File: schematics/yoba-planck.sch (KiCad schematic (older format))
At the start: 54 parts, among them M1 AUDIO-JACK3, M2 AUDIO-JACK3, M3 ARDUINO_PRO_MICRO, SW1 SW_PUSH, SW10 SW_PUSH, SW11 SW_PUSH, SW12 SW_PUSH, SW13 SW_PUSH, SW14 SW_PUSH, SW15 SW_PUSH, SW16 SW_PUSH, SW17 SW_PUSH, SW18 SW_PUSH, SW19 SW_PUSH, SW2 SW_PUSH, SW20 SW_PUSH, SW21 SW_PUSH, SW22 SW_PUSH, SW23 SW_PUSH, SW24 SW_PUSH, SW3 SW_PUSH, SW4 SW_PUSH, SW5 SW_PUSH, SW6 SW_PUSH, SW7 SW_PUSH, SW8 SW_PUSH, SW9 SW_PUSH

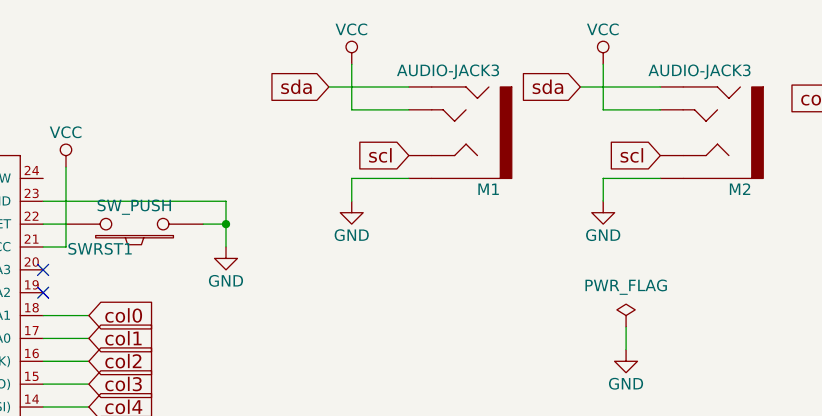
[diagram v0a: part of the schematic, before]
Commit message: series resistance added to i2c bus
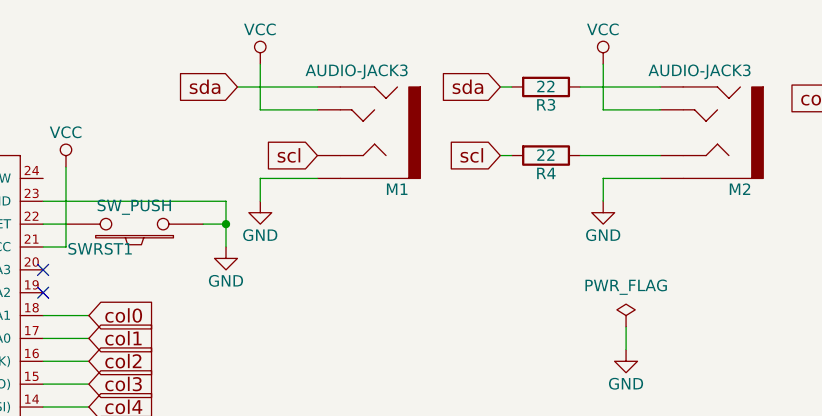
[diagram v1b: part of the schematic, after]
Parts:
- added R3, R4: 22, symbol R
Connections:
- net scl: now also R4.2; no longer M2.3 (RNG1)
- net sda: now also R3.2; no longer M2.2 (RNG2)
- new net: M2.2 (RNG2), R3.1
- new net: M2.3 (RNG1), R4.1
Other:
- moved on the sheet: M1
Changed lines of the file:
@@
 $EndComp
 $Comp
-L GND #PWR01
+L GND #PWR3
 U 1 1 58C7AB40
 P 4100 1500
-F 0 "#PWR01" H 4100 1250 50  0001 C CNN
+F 0 "#PWR3" H 4100 1250 50  0001 C CNN
 F 1 "GND" H 4100 1350 50  0000 C CNN
 F 2 "" H 4100 1500 50  0000 C CNN
@@
 $EndComp
 $Comp
-L VCC #PWR02
+L VCC #PWR4
 U 1 1 58C80AC6
-P 4650 700
-F 0 "#PWR02" H 4650 550 50  0001 C CNN
-F 1 "VCC" H 4650 850 50  0000 C CNN
-F 2 "" H 4650 700 50  0000 C CNN
-F 3 "" H 4650 700 50  0000 C CNN
-	1    4650 700
-	1    0    0    -1
-$EndComp
-Wire Wire Line
-	4650 700  4650 900
-$Comp
-L GND #PWR03
+P 4250 700
+F 0 "#PWR4" H 4250 550 50  0001 C CNN
+F 1 "VCC" H 4250 850 50  0000 C CNN
+F 2 "" H 4250 700 50  0000 C CNN
+F 3 "" H 4250 700 50  0000 C CNN
+	1    4250 700
+	1    0    0    -1
+$EndComp
+Wire Wire Line
+	4250 700  4250 900
+$Comp
+L GND #PWR5
 U 1 1 58C80C56
-P 4650 1300
-F 0 "#PWR03" H 4650 1050 50  0001 C CNN
-F 1 "GND" H 4650 1150 50  0000 C CNN
-F 2 "" H 4650 1300 50  0000 C CNN
-F 3 "" H 4650 1300 50  0000 C CNN
-	1    4650 1300
-	1    0    0    -1
-$EndComp
-Wire Wire Line
-	4900 1200 4650 1200
-Wire Wire Line
-	4650 1200 4650 1300
+P 4250 1300
+F 0 "#PWR5" H 4250 1050 50  0001 C CNN
+F 1 "GND" H 4250 1150 50  0000 C CNN
+F 2 "" H 4250 1300 50  0000 C CNN
+F 3 "" H 4250 1300 50  0000 C CNN
+	1    4250 1300
+	1    0    0    -1
+$EndComp
+Wire Wire Line
+	4500 1200 4250 1200
+Wire Wire Line
+	4250 1200 4250 1300
 Text GLabel 1950 1600 0    60   Input ~ 0
 sda
-Text GLabel 4900 1100 0    60   Input ~ 0
+Text GLabel 4500 1100 0    60   Input ~ 0
 scl
-Text GLabel 4550 800  0    60   Input ~ 0
+Text GLabel 4150 800  0    60   Input ~ 0
 sda
 $Comp
-L GND #PWR04
+L GND #PWR8
 U 1 1 58C8646C
 P 5850 1950
-F 0 "#PWR04" H 5850 1700 50  0001 C CNN
+F 0 "#PWR8" H 5850 1700 50  0001 C CNN
 F 1 "GND" H 5850 1800 50  0000 C CNN
 F 2 "" H 5850 1950 50  0000 C CNN
@@
 $EndComp
 $Comp
-L PWR_FLAG #FLG05
+L PWR_FLAG #FLG1
 U 1 1 58C86543
 P 5850 1850
-F 0 "#FLG05" H 5850 1945 50  0001 C CNN
+F 0 "#FLG1" H 5850 1945 50  0001 C CNN
 F 1 "PWR_FLAG" H 5850 2030 50  0000 C CNN
 F 2 "" H 5850 1850 50  0000 C CNN
@@
 	5850 1850 5850 1950
 Wire Wire Line
-	4650 900  4900 900
-Wire Wire Line
-	4550 800  4900 800
+	4250 900  4500 900
+Wire Wire Line
+	4150 800  4500 800
 $Comp
 L AUDIO-JACK3 M1
 U 1 1 58C9EB5E
-P 5100 1000
-F 0 "M1" H 4900 1220 50  0000 L BNN
-F 1 "AUDIO-JACK3" H 4900 700 50  0000 L BNN
-F 2 "yoba:TRRS-ebay" H 5130 1150 20  0001 C CNN
-F 3 "" H 5100 1000 60  0001 C CNN
-	1    5100 1000
+P 4700 1000
+F 0 "M1" H 4500 1220 50  0000 L BNN
+F 1 "AUDIO-JACK3" H 4500 700 50  0000 L BNN
+F 2 "yoba:TRRS-ebay" H 4730 1150 20  0001 C CNN
+F 3 "" H 4700 1000 60  0001 C CNN
+	1    4700 1000
 	-1   0    0    1
 $EndComp
@@
 	1950 1700 2400 1700
 $Comp
-L VCC #PWR06
+L VCC #PWR1
 U 1 1 58CA693D
 P 2100 1050
-F 0 "#PWR06" H 2100 900 50  0001 C CNN
+F 0 "#PWR1" H 2100 900 50  0001 C CNN
 F 1 "VCC" H 2100 1200 50  0000 C CNN
 F 2 "" H 2100 1050 50  0000 C CNN
@@
 Connection ~ 2100 1150
 $Comp
-L VCC #PWR07
+L VCC #PWR2
 U 1 1 58CA85FA
 P 3400 1150
-F 0 "#PWR07" H 3400 1000 50  0001 C CNN
+F 0 "#PWR2" H 3400 1000 50  0001 C CNN
 F 1 "VCC" H 3400 1300 50  0000 C CNN
 F 2 "" H 3400 1150 50  0000 C CNN
@@
 NoConn ~ 2400 1800
 $Comp
-L VCC #PWR08
+L VCC #PWR6
 U 1 1 58D178D3
 P 5750 700
-F 0 "#PWR08" H 5750 550 50  0001 C CNN
+F 0 "#PWR6" H 5750 550 50  0001 C CNN
 F 1 "VCC" H 5750 850 50  0000 C CNN
 F 2 "" H 5750 700 50  0000 C CNN
@@
 	5750 700  5750 900
 $Comp
-L GND #PWR09
+L GND #PWR7
 U 1 1 58D178DA
 P 5750 1300
-F 0 "#PWR09" H 5750 1050 50  0001 C CNN
+F 0 "#PWR7" H 5750 1050 50  0001 C CNN
 F 1 "GND" H 5750 1150 50  0000 C CNN
 F 2 "" H 5750 1300 50  0000 C CNN
@@
 Wire Wire Line
 	5750 1200 5750 1300
-Text GLabel 6000 1100 0    60   Input ~ 0
+Text GLabel 5300 1100 0    60   Input ~ 0
 scl
-Text GLabel 5650 800  0    60   Input ~ 0
+Text GLabel 5300 800  0    60   Input ~ 0
 sda
 Wire Wire Line
@@
 $EndComp
 NoConn ~ 2400 1900
+$Comp
+L R R3
+U 1 1 58DBF535
+P 5500 800
+F 0 "R3" V 5580 800 50  0000 C CNN
+F 1 "22" V 5500 800 50  0000 C CNN
+F 2 "" V 5430 800 50  0000 C CNN
+F 3 "" H 5500 800 50  0000 C CNN
+	1    5500 800
+	0    1    1    0
+$EndComp
+Wire Wire Line
+	5350 800  5300 800
+$Comp
+L R R4
+U 1 1 58DBFD81
+P 5500 1100
+F 0 "R4" V 5580 1100 50  0000 C CNN
+F 1 "22" V 5500 1100 50  0000 C CNN
+F 2 "" V 5430 1100 50  0000 C CNN
+F 3 "" H 5500 1100 50  0000 C CNN
+	1    5500 1100
+	0    1    1    0
+$EndComp
+Wire Wire Line
+	5300 1100 5350 1100
+Wire Wire Line
+	5650 1100 6000 1100
 $EndSCHEMATC

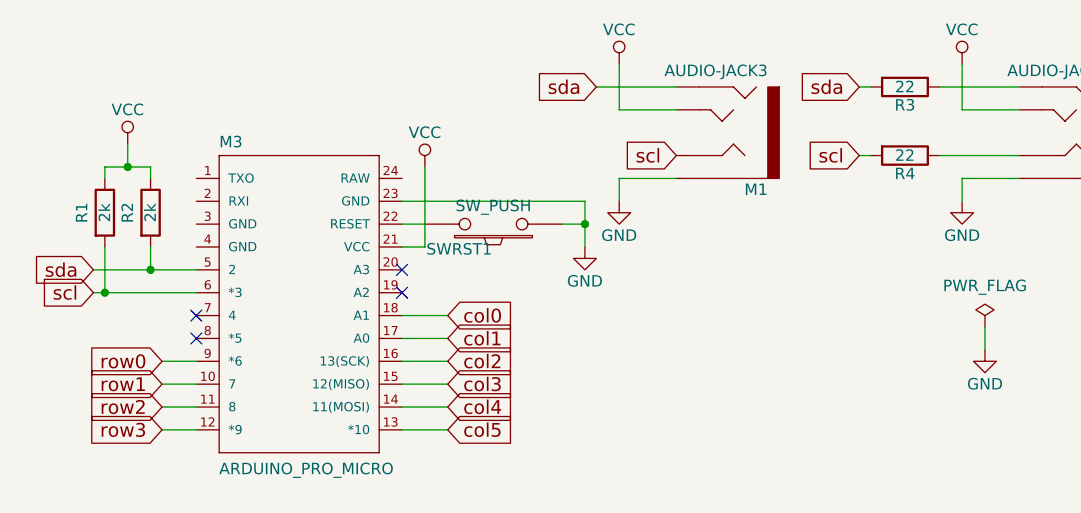
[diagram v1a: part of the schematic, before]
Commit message: Logo updated, layout improoved, mouting holes enlarged
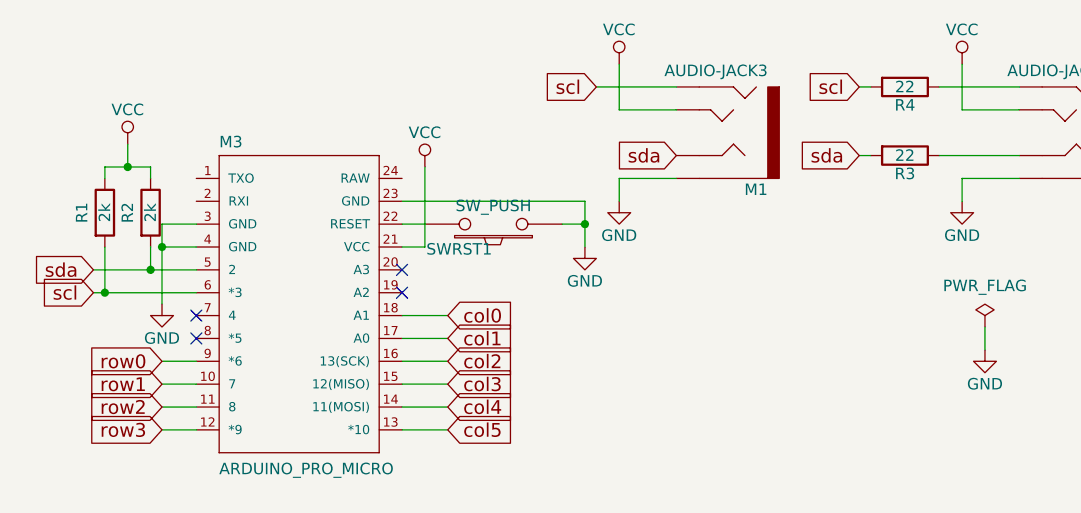
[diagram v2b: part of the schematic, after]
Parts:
- M3: footprint SparkFun-Boards:ARDUINO_PRO_MICRO -> yoba:ARDUINO_PRO_MICRO
- R3, R4: footprint (none) -> Resistors_SMD:R_0805_HandSoldering
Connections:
- net GND: now also M3.3 (GND), M3.4 (GND)
- net scl: now also M1.2 (RNG2); no longer M1.3 (RNG1)
- net sda: now also M1.3 (RNG1); no longer M1.2 (RNG2)
- net at M2.2 (RNG2): now also R4.1; no longer R3.1
- net at M2.3 (RNG1): now also R3.1; no longer R4.1
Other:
- moved on the sheet: R3, R4
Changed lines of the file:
@@
 $EndComp
 $Comp
-L GND #PWR3
+L GND #PWR01
 U 1 1 58C7AB40
 P 4100 1500
-F 0 "#PWR3" H 4100 1250 50  0001 C CNN
+F 0 "#PWR01" H 4100 1250 50  0001 C CNN
 F 1 "GND" H 4100 1350 50  0000 C CNN
 F 2 "" H 4100 1500 50  0000 C CNN
@@
 $EndComp
 $Comp
-L VCC #PWR4
+L VCC #PWR02
 U 1 1 58C80AC6
 P 4250 700
-F 0 "#PWR4" H 4250 550 50  0001 C CNN
+F 0 "#PWR02" H 4250 550 50  0001 C CNN
 F 1 "VCC" H 4250 850 50  0000 C CNN
 F 2 "" H 4250 700 50  0000 C CNN
@@
 	4250 700  4250 900
 $Comp
-L GND #PWR5
+L GND #PWR03
 U 1 1 58C80C56
 P 4250 1300
-F 0 "#PWR5" H 4250 1050 50  0001 C CNN
+F 0 "#PWR03" H 4250 1050 50  0001 C CNN
 F 1 "GND" H 4250 1150 50  0000 C CNN
 F 2 "" H 4250 1300 50  0000 C CNN
@@
 Text GLabel 1950 1600 0    60   Input ~ 0
 sda
+Text GLabel 4150 800  0    60   Input ~ 0
+scl
 Text GLabel 4500 1100 0    60   Input ~ 0
-scl
-Text GLabel 4150 800  0    60   Input ~ 0
 sda
 $Comp
-L GND #PWR8
+L GND #PWR04
 U 1 1 58C8646C
 P 5850 1950
-F 0 "#PWR8" H 5850 1700 50  0001 C CNN
+F 0 "#PWR04" H 5850 1700 50  0001 C CNN
 F 1 "GND" H 5850 1800 50  0000 C CNN
 F 2 "" H 5850 1950 50  0000 C CNN
@@
 $EndComp
 $Comp
-L PWR_FLAG #FLG1
+L PWR_FLAG #FLG05
 U 1 1 58C86543
 P 5850 1850
-F 0 "#FLG1" H 5850 1945 50  0001 C CNN
+F 0 "#FLG05" H 5850 1945 50  0001 C CNN
 F 1 "PWR_FLAG" H 5850 2030 50  0000 C CNN
 F 2 "" H 5850 1850 50  0000 C CNN
@@
 	1950 1700 2400 1700
 $Comp
-L VCC #PWR1
+L VCC #PWR06
 U 1 1 58CA693D
 P 2100 1050
-F 0 "#PWR1" H 2100 900 50  0001 C CNN
+F 0 "#PWR06" H 2100 900 50  0001 C CNN
 F 1 "VCC" H 2100 1200 50  0000 C CNN
 F 2 "" H 2100 1050 50  0000 C CNN
@@
 Connection ~ 2100 1150
 $Comp
-L VCC #PWR2
+L VCC #PWR07
 U 1 1 58CA85FA
 P 3400 1150
-F 0 "#PWR2" H 3400 1000 50  0001 C CNN
+F 0 "#PWR07" H 3400 1000 50  0001 C CNN
 F 1 "VCC" H 3400 1300 50  0000 C CNN
 F 2 "" H 3400 1150 50  0000 C CNN
@@
 NoConn ~ 2400 1800
 $Comp
-L VCC #PWR6
+L VCC #PWR08
 U 1 1 58D178D3
 P 5750 700
-F 0 "#PWR6" H 5750 550 50  0001 C CNN
+F 0 "#PWR08" H 5750 550 50  0001 C CNN
 F 1 "VCC" H 5750 850 50  0000 C CNN
 F 2 "" H 5750 700 50  0000 C CNN
@@
 	5750 700  5750 900
 $Comp
-L GND #PWR7
+L GND #PWR09
 U 1 1 58D178DA
 P 5750 1300
-F 0 "#PWR7" H 5750 1050 50  0001 C CNN
+F 0 "#PWR09" H 5750 1050 50  0001 C CNN
 F 1 "GND" H 5750 1150 50  0000 C CNN
 F 2 "" H 5750 1300 50  0000 C CNN
@@
 Wire Wire Line
 	5750 1200 5750 1300
+Text GLabel 5300 800  0    60   Input ~ 0
+scl
 Text GLabel 5300 1100 0    60   Input ~ 0
-scl
-Text GLabel 5300 800  0    60   Input ~ 0
 sda
 Wire Wire Line
@@
 F 0 "M3" H 2500 2530 50  0000 L BNN
 F 1 "ARDUINO_PRO_MICRO" H 2500 1100 50  0000 L BNN
-F 2 "SparkFun-Boards:ARDUINO_PRO_MICRO" H 2830 1950 20  0001 C CNN
+F 2 "yoba:ARDUINO_PRO_MICRO" H 2830 1950 20  0001 C CNN
 F 3 "" H 2800 1800 60  0001 C CNN
 	1    2800 1800
@@
 L R R3
 U 1 1 58DBF535
+P 5500 1100
+F 0 "R3" V 5580 1100 50  0000 C CNN
+F 1 "22" V 5500 1100 50  0000 C CNN
+F 2 "Resistors_SMD:R_0805_HandSoldering" V 5430 1100 50  0001 C CNN
+F 3 "" H 5500 1100 50  0000 C CNN
+	1    5500 1100
+	0    1    1    0
+$EndComp
+Wire Wire Line
+	5350 800  5300 800
+$Comp
+L R R4
+U 1 1 58DBFD81
 P 5500 800
-F 0 "R3" V 5580 800 50  0000 C CNN
+F 0 "R4" V 5580 800 50  0000 C CNN
 F 1 "22" V 5500 800 50  0000 C CNN
-F 2 "" V 5430 800 50  0000 C CNN
+F 2 "Resistors_SMD:R_0805_HandSoldering" V 5430 800 50  0001 C CNN
 F 3 "" H 5500 800 50  0000 C CNN
 	1    5500 800
@@
 $EndComp
 Wire Wire Line
-	5350 800  5300 800
-$Comp
-L R R4
-U 1 1 58DBFD81
-P 5500 1100
-F 0 "R4" V 5580 1100 50  0000 C CNN
-F 1 "22" V 5500 1100 50  0000 C CNN
-F 2 "" V 5430 1100 50  0000 C CNN
-F 3 "" H 5500 1100 50  0000 C CNN
-	1    5500 1100
-	0    1    1    0
-$EndComp
-Wire Wire Line
 	5300 1100 5350 1100
 Wire Wire Line
 	5650 1100 6000 1100
+$Comp
+L GND #PWR010
+U 1 1 58DC02E5
+P 2250 1750
+F 0 "#PWR010" H 2250 1500 50  0001 C CNN
+F 1 "GND" H 2250 1600 50  0000 C CNN
+F 2 "" H 2250 1750 50  0000 C CNN
+F 3 "" H 2250 1750 50  0000 C CNN
+	1    2250 1750
+	1    0    0    -1
+$EndComp
+Wire Wire Line
+	2400 1400 2250 1400
+Wire Wire Line
+	2250 1400 2250 1750
+Wire Wire Line
+	2400 1500 2250 1500
+Connection ~ 2250 1500
 $EndSCHEMATC

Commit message: rev2
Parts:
- added C1: C, Capacitors_SMD:C_0805_HandSoldering, symbol C
- added D25, D26, D27, D28, D29, D30, D31, D32, D33, D34, D35, D36, D37, D38, D39, D40, D41, D42, D43, D44, D45, D46, D47, D48: LED, mx1a:MX1A-led, symbol LED
- added Q1: BS170, TO_SOT_Packages_SMD:SOT-23_Handsoldering, symbol BS170
- added R10, R11, R12, R13, R14, R15, R16, R17, R18, R19, R20, R21, R22, R23, R24, R25, R26, R27, R28, R5, R6, R7, R8, R9: 1k, Resistors_SMD:R_0805_HandSoldering, symbol R
- renumbered SWRST1 to RST1
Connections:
- net GND: now also C1.1, Q1.3 (S)
- net VCC: now also D25.2 (A), D26.2 (A), D27.2 (A), D28.2 (A), D29.2 (A), D30.2 (A), D31.2 (A), D32.2 (A), D33.2 (A), D34.2 (A), D35.2 (A), D36.2 (A), D37.2 (A), D38.2 (A), D39.2 (A), D40.2 (A), D41.2 (A), D42.2 (A), D43.2 (A), D44.2 (A), D45.2 (A), D46.2 (A), D47.2 (A), D48.2 (A)
- net row0: now also D1.1 (K), D13.1 (K), D17.1 (K), D21.1 (K), D5.1 (K), D9.1 (K); no longer D1.2 (A), D13.2 (A), D17.2 (A), D21.2 (A), D5.2 (A), D9.2 (A)
- net row1: now also D10.1 (K), D14.1 (K), D18.1 (K), D2.1 (K), D22.1 (K), D6.1 (K); no longer D10.2 (A), D14.2 (A), D18.2 (A), D2.2 (A), D22.2 (A), D6.2 (A)
- net row2: now also D11.1 (K), D15.1 (K), D19.1 (K), D23.1 (K), D3.1 (K), D7.1 (K); no longer D11.2 (A), D15.2 (A), D19.2 (A), D23.2 (A), D3.2 (A), D7.2 (A)
- net row3: now also D12.1 (K), D16.1 (K), D20.1 (K), D24.1 (K), D4.1 (K), D8.1 (K); no longer D12.2 (A), D16.2 (A), D20.2 (A), D24.2 (A), D4.2 (A), D8.2 (A)
- net scl: no longer M1.2 (RNG2), R1.2
- net sda: no longer M1.3 (RNG1), R2.2
- net at SW1.2: now also D1.2 (A); no longer D1.1 (K)
- net at SW5.2: now also D5.2 (A); no longer D5.1 (K)
- net at SW9.2: now also D9.2 (A); no longer D9.1 (K)
- net at SW13.2: now also D13.2 (A); no longer D13.1 (K)
- net at SW17.2: now also D17.2 (A); no longer D17.1 (K)
- net at SW21.2: now also D21.2 (A); no longer D21.1 (K)
- net at SW2.2: now also D2.2 (A); no longer D2.1 (K)
- net at SW6.2: now also D6.2 (A); no longer D6.1 (K)
- net at SW10.2: now also D10.2 (A); no longer D10.1 (K)
- net at SW14.2: now also D14.2 (A); no longer D14.1 (K)
- net at SW18.2: now also D18.2 (A); no longer D18.1 (K)
- net at SW22.2: now also D22.2 (A); no longer D22.1 (K)
- net at SW3.2: now also D3.2 (A); no longer D3.1 (K)
- net at SW7.2: now also D7.2 (A); no longer D7.1 (K)
- net at SW11.2: now also D11.2 (A); no longer D11.1 (K)
- net at SW15.2: now also D15.2 (A); no longer D15.1 (K)
- net at SW19.2: now also D19.2 (A); no longer D19.1 (K)
- net at SW23.2: now also D23.2 (A); no longer D23.1 (K)
- net at SW4.2: now also D4.2 (A); no longer D4.1 (K)
- net at SW8.2: now also D8.2 (A); no longer D8.1 (K)
- net at SW12.2: now also D12.2 (A); no longer D12.1 (K)
- net at SW16.2: now also D16.2 (A); no longer D16.1 (K)
- net at SW20.2: now also D20.2 (A); no longer D20.1 (K)
- net at SW24.2: now also D24.2 (A); no longer D24.1 (K)
- net at M3.22 (RESET), RST1.2: now also C1.2
- net backlight: now reaches M3.8 (*5)
- net backlight: now also Q1.2 (G)
- net at M2.2 (RNG2), R4.1: now also M1.2 (RNG2), R1.2
- net at M2.3 (RNG1), R3.1: now also M1.3 (RNG1), R2.2
- new net: D25.1 (K), R5.2
- new net: Q1.1 (D), R10.1, R11.1, R12.1, R13.1, R14.1, R15.1, R16.1, R17.1, R18.1, R19.1, R20.1, R21.1, R22.1, R23.1, R24.1, R25.1, R26.1, R27.1, R28.1, R5.1, R6.1, R7.1, R8.1, R9.1
- new net: D26.1 (K), R6.2
- new net: D27.1 (K), R7.2
- new net: D28.1 (K), R8.2
- new net: D29.1 (K), R9.2
- new net: D30.1 (K), R10.2
- new net: D31.1 (K), R11.2
- new net: D32.1 (K), R12.2
- new net: D33.1 (K), R13.2
- new net: D34.1 (K), R14.2
- new net: D35.1 (K), R15.2
- new net: D36.1 (K), R16.2
- new net: D37.1 (K), R17.2
- new net: D38.1 (K), R18.2
- new net: D39.1 (K), R19.2
- new net: D40.1 (K), R20.2
- new net: D41.1 (K), R21.2
- new net: D42.1 (K), R22.2
- new net: D43.1 (K), R23.2
- new net: D44.1 (K), R24.2
- new net: D45.1 (K), R25.2
- new net: D46.1 (K), R26.2
- new net: D47.1 (K), R27.2
- new net: D48.1 (K), R28.2
- no-connect marks 4 -> 3
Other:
- moved on the sheet: M1, M2, R1, R2, R3, R4
